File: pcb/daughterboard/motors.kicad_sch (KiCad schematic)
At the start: 20 parts, among them J10 Conn_01x04_Socket, J11 Conn_01x04_Socket, J12 Conn_01x04_Socket, J13 Conn_01x04_Socket, J14 Conn_01x04_Socket, J15 Conn_01x04_Socket, J16 Conn_01x04_Socket, J17 Conn_01x04_Socket, J18 Conn_01x04_Socket, J19 Conn_01x04_Socket, J2 Conn_01x04_Socket, J20 Conn_01x04_Socket, J21 Conn_01x04_Socket, J3 Conn_01x04_Socket, J4 Conn_01x04_Socket, J5 Conn_01x04_Socket, J6 Conn_01x04_Socket, J7 Conn_01x04_Socket, J8 Conn_01x04_Socket, J9 Conn_01x04_Socket

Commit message: added initial power lines
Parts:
- removed J2: Conn_01x04_Socket, A_HANU_FOOTPRINTS:52207-0633, symbol Connector:Conn_01x04_Socket
- added J22: Conn_01x04_Socket, A_HANU_FOOTPRINTS:52207-0633, symbol Connector:Conn_01x04_Socket
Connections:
- net PAD1_M1: now also J3.1 (Pin_1)
- net PAD1_M10: now also J12.1 (Pin_1); no longer J11.1 (Pin_1)
- net PAD1_M11: now also J13.1 (Pin_1); no longer J12.1 (Pin_1)
- net PAD1_M12: now also J14.1 (Pin_1); no longer J13.1 (Pin_1)
- net PAD1_M13: now also J15.1 (Pin_1); no longer J14.1 (Pin_1)
- net PAD1_M14: now also J16.1 (Pin_1); no longer J15.1 (Pin_1)
- net PAD1_M15: now also J17.1 (Pin_1); no longer J16.1 (Pin_1)
- net PAD1_M16: now also J18.1 (Pin_1); no longer J17.1 (Pin_1)
- net PAD1_M17: now also J19.1 (Pin_1); no longer J18.1 (Pin_1)
- net PAD1_M18: now also J20.1 (Pin_1); no longer J19.1 (Pin_1)
- net PAD1_M19: now also J21.1 (Pin_1); no longer J20.1 (Pin_1)
- net PAD1_M2: now also J4.1 (Pin_1); no longer J3.1 (Pin_1)
- net PAD1_M20: now also J22.1 (Pin_1); no longer J21.1 (Pin_1)
- net PAD1_M3: now also J5.1 (Pin_1); no longer J4.1 (Pin_1)
- net PAD1_M4: now also J6.1 (Pin_1); no longer J5.1 (Pin_1)
- net PAD1_M5: now also J7.1 (Pin_1); no longer J6.1 (Pin_1)
- net PAD1_M6: now also J8.1 (Pin_1); no longer J7.1 (Pin_1)
- net PAD1_M7: now also J9.1 (Pin_1); no longer J8.1 (Pin_1)
- net PAD1_M8: now also J10.1 (Pin_1); no longer J9.1 (Pin_1)
- net PAD1_M9: now also J11.1 (Pin_1); no longer J10.1 (Pin_1)
- net PAD2_M1: now also J3.2 (Pin_2)
- net PAD2_M10: now also J12.2 (Pin_2); no longer J11.2 (Pin_2)
- net PAD2_M11: now also J13.2 (Pin_2); no longer J12.2 (Pin_2)
- net PAD2_M12: now also J14.2 (Pin_2); no longer J13.2 (Pin_2)
- net PAD2_M13: now also J15.2 (Pin_2); no longer J14.2 (Pin_2)
- net PAD2_M14: now also J16.2 (Pin_2); no longer J15.2 (Pin_2)
- net PAD2_M15: now also J17.2 (Pin_2); no longer J16.2 (Pin_2)
- net PAD2_M16: now also J18.2 (Pin_2); no longer J17.2 (Pin_2)
- net PAD2_M17: now also J19.2 (Pin_2); no longer J18.2 (Pin_2)
- net PAD2_M18: now also J20.2 (Pin_2); no longer J19.2 (Pin_2)
- net PAD2_M19: now also J21.2 (Pin_2); no longer J20.2 (Pin_2)
- net PAD2_M2: now also J4.2 (Pin_2); no longer J3.2 (Pin_2)
- net PAD2_M20: now also J22.2 (Pin_2); no longer J21.2 (Pin_2)
- net PAD2_M3: now also J5.2 (Pin_2); no longer J4.2 (Pin_2)
- net PAD2_M4: now also J6.2 (Pin_2); no longer J5.2 (Pin_2)
- net PAD2_M5: now also J7.2 (Pin_2); no longer J6.2 (Pin_2)
- net PAD2_M6: now also J8.2 (Pin_2); no longer J7.2 (Pin_2)
- net PAD2_M7: now also J9.2 (Pin_2); no longer J8.2 (Pin_2)
- net PAD2_M8: now also J10.2 (Pin_2); no longer J9.2 (Pin_2)
- net PAD2_M9: now also J11.2 (Pin_2); no longer J10.2 (Pin_2)
- net PAD3_M1: now also J3.3 (Pin_3)
- net PAD3_M10: now also J12.3 (Pin_3); no longer J11.3 (Pin_3)
- net PAD3_M11: now also J13.3 (Pin_3); no longer J12.3 (Pin_3)
- net PAD3_M12: now also J14.3 (Pin_3); no longer J13.3 (Pin_3)
- net PAD3_M13: now also J15.3 (Pin_3); no longer J14.3 (Pin_3)
- net PAD3_M14: now also J16.3 (Pin_3); no longer J15.3 (Pin_3)
- net PAD3_M15: now also J17.3 (Pin_3); no longer J16.3 (Pin_3)
- net PAD3_M16: now also J18.3 (Pin_3); no longer J17.3 (Pin_3)
- net PAD3_M17: now also J19.3 (Pin_3); no longer J18.3 (Pin_3)
- net PAD3_M18: now also J20.3 (Pin_3); no longer J19.3 (Pin_3)
- net PAD3_M19: now also J21.3 (Pin_3); no longer J20.3 (Pin_3)
- net PAD3_M2: now also J4.3 (Pin_3); no longer J3.3 (Pin_3)
- net PAD3_M20: now also J22.3 (Pin_3); no longer J21.3 (Pin_3)
- net PAD3_M3: now also J5.3 (Pin_3); no longer J4.3 (Pin_3)
- net PAD3_M4: now also J6.3 (Pin_3); no longer J5.3 (Pin_3)
- net PAD3_M5: now also J7.3 (Pin_3); no longer J6.3 (Pin_3)
- net PAD3_M6: now also J8.3 (Pin_3); no longer J7.3 (Pin_3)
- net PAD3_M7: now also J9.3 (Pin_3); no longer J8.3 (Pin_3)
- net PAD3_M8: now also J10.3 (Pin_3); no longer J9.3 (Pin_3)
- net PAD3_M9: now also J11.3 (Pin_3); no longer J10.3 (Pin_3)
- net PAD4_M1: now also J3.4 (Pin_4)
- net PAD4_M10: now also J12.4 (Pin_4); no longer J11.4 (Pin_4)
- net PAD4_M11: now also J13.4 (Pin_4); no longer J12.4 (Pin_4)
- net PAD4_M12: now also J14.4 (Pin_4); no longer J13.4 (Pin_4)
- net PAD4_M13: now also J15.4 (Pin_4); no longer J14.4 (Pin_4)
- net PAD4_M14: now also J16.4 (Pin_4); no longer J15.4 (Pin_4)
- net PAD4_M15: now also J17.4 (Pin_4); no longer J16.4 (Pin_4)
- net PAD4_M16: now also J18.4 (Pin_4); no longer J17.4 (Pin_4)
- net PAD4_M17: now also J19.4 (Pin_4); no longer J18.4 (Pin_4)
- net PAD4_M18: now also J20.4 (Pin_4); no longer J19.4 (Pin_4)
- net PAD4_M19: now also J21.4 (Pin_4); no longer J20.4 (Pin_4)
- net PAD4_M2: now also J4.4 (Pin_4); no longer J3.4 (Pin_4)
- net PAD4_M20: now also J22.4 (Pin_4); no longer J21.4 (Pin_4)
- net PAD4_M3: now also J5.4 (Pin_4); no longer J4.4 (Pin_4)
- net PAD4_M4: now also J6.4 (Pin_4); no longer J5.4 (Pin_4)
- net PAD4_M5: now also J7.4 (Pin_4); no longer J6.4 (Pin_4)
- net PAD4_M6: now also J8.4 (Pin_4); no longer J7.4 (Pin_4)
- net PAD4_M7: now also J9.4 (Pin_4); no longer J8.4 (Pin_4)
- net PAD4_M8: now also J10.4 (Pin_4); no longer J9.4 (Pin_4)
- net PAD4_M9: now also J11.4 (Pin_4); no longer J10.4 (Pin_4)

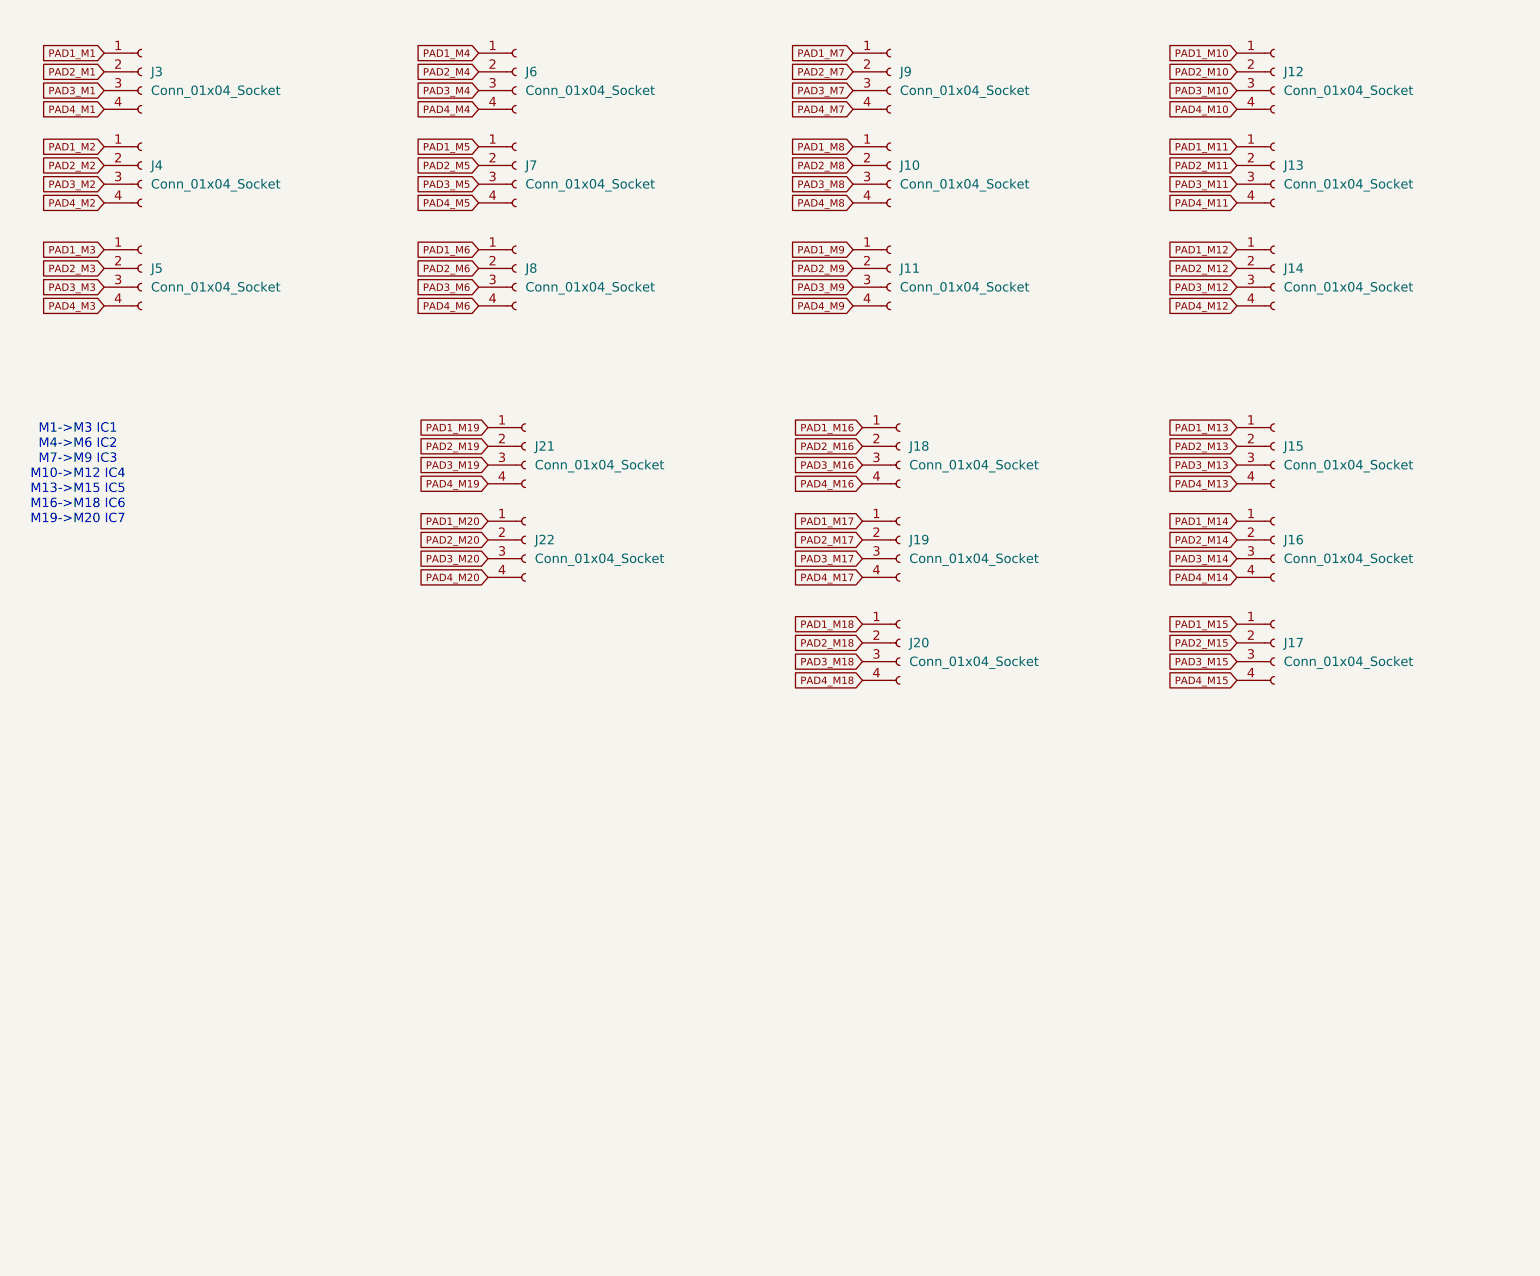
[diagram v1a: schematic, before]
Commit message: added routes for some motor-connectors
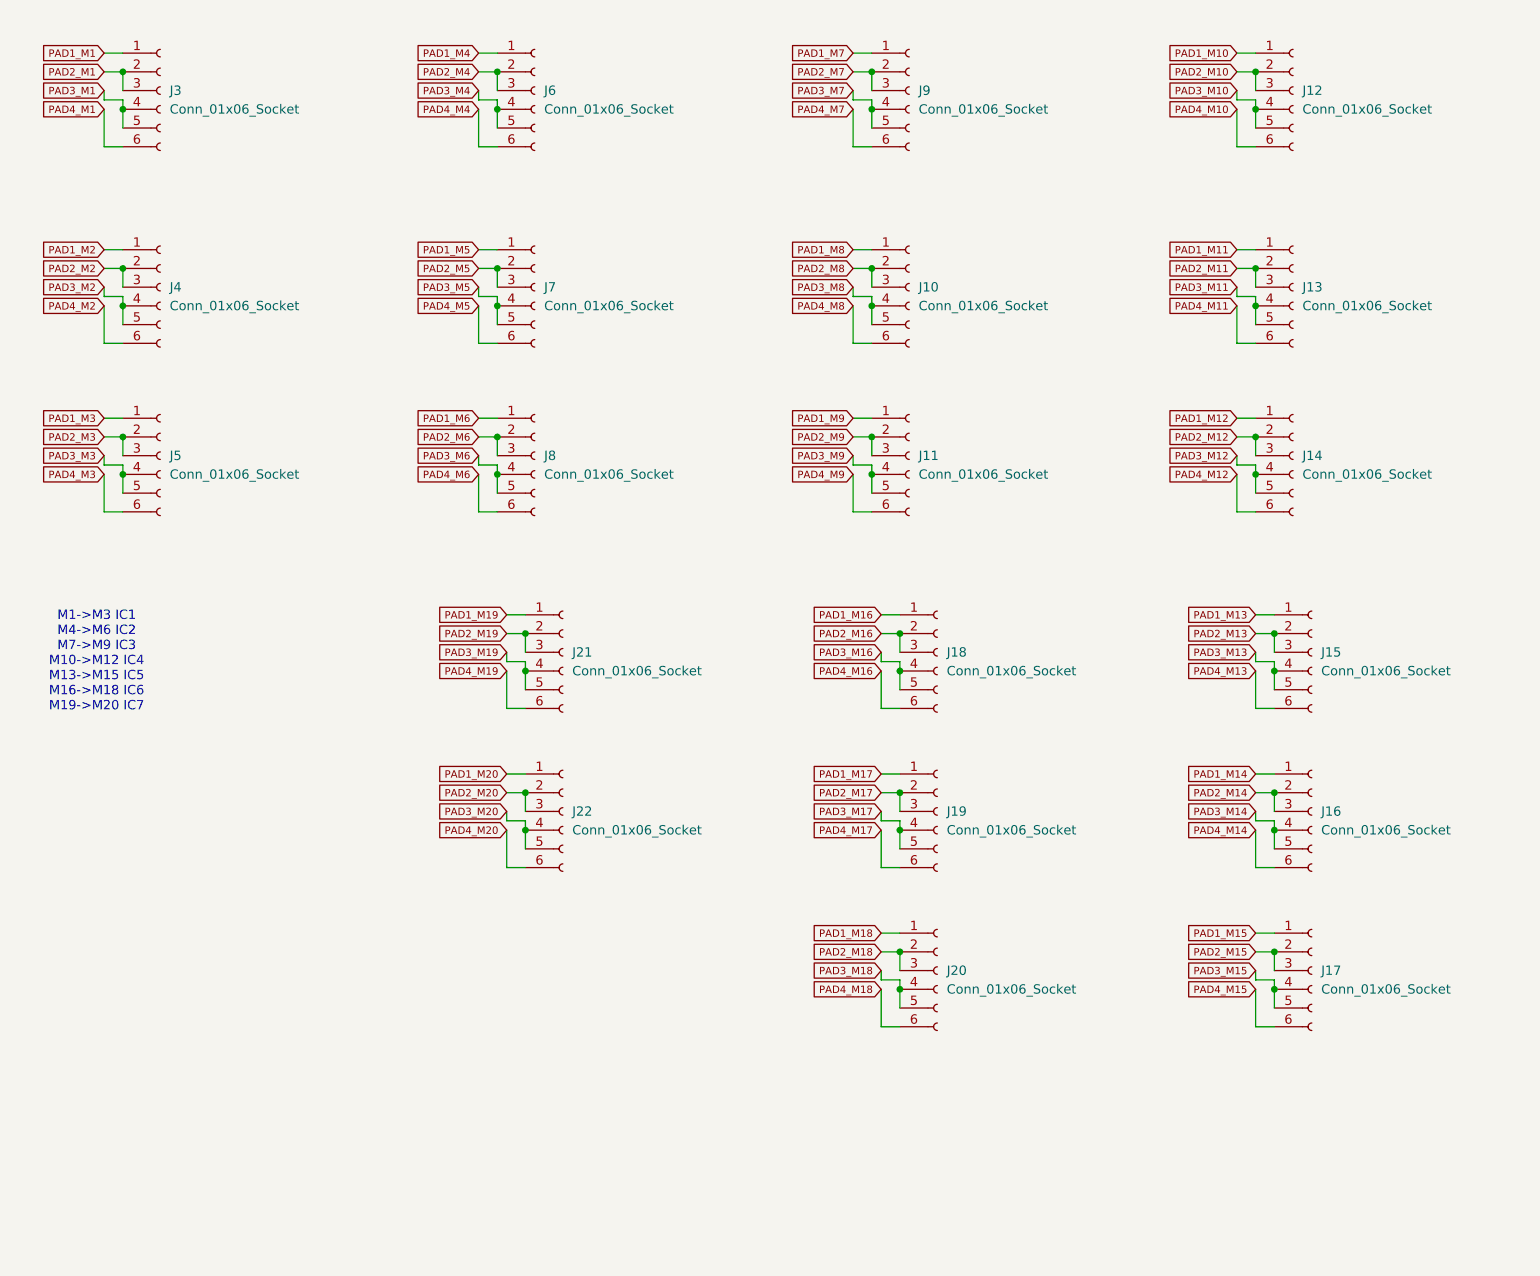
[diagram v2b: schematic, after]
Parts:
- removed J10, J11, J12, J13, J14, J15, J16, J17, J18, J19, J20, J21, J22, J3, J4, J5, J6, J7, J8, J9: Conn_01x04_Socket, A_HANU_FOOTPRINTS:52207-0633, symbol Connector:Conn_01x04_Socket
- added J10, J11, J12, J13, J14, J15, J16, J17, J18, J19, J20, J21, J22, J3, J4, J5, J6, J7, J8, J9: Conn_01x06_Socket, A_HANU_FOOTPRINTS:52207-0633, symbol Connector:Conn_01x06_Socket
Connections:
- net PAD1_M1: now also J3.1 (Pin_1)
- net PAD1_M10: now also J12.1 (Pin_1)
- net PAD1_M11: now also J13.1 (Pin_1)
- net PAD1_M12: now also J14.1 (Pin_1)
- net PAD1_M13: now also J15.1 (Pin_1)
- net PAD1_M14: now also J16.1 (Pin_1)
- net PAD1_M15: now also J17.1 (Pin_1)
- net PAD1_M16: now also J18.1 (Pin_1)
- net PAD1_M17: now also J19.1 (Pin_1)
- net PAD1_M18: now also J20.1 (Pin_1)
- net PAD1_M19: now also J21.1 (Pin_1)
- net PAD1_M2: now also J4.1 (Pin_1)
- net PAD1_M20: now also J22.1 (Pin_1)
- net PAD1_M3: now also J5.1 (Pin_1)
- net PAD1_M4: now also J6.1 (Pin_1)
- net PAD1_M5: now also J7.1 (Pin_1)
- net PAD1_M6: now also J8.1 (Pin_1)
- net PAD1_M7: now also J9.1 (Pin_1)
- net PAD1_M8: now also J10.1 (Pin_1)
- net PAD1_M9: now also J11.1 (Pin_1)
- net PAD2_M1: now also J3.2 (Pin_2), J3.3 (Pin_3)
- net PAD2_M10: now also J12.2 (Pin_2), J12.3 (Pin_3)
- net PAD2_M11: now also J13.2 (Pin_2), J13.3 (Pin_3)
- net PAD2_M12: now also J14.2 (Pin_2), J14.3 (Pin_3)
- net PAD2_M13: now also J15.2 (Pin_2), J15.3 (Pin_3)
- net PAD2_M14: now also J16.2 (Pin_2), J16.3 (Pin_3)
- net PAD2_M15: now also J17.2 (Pin_2), J17.3 (Pin_3)
- net PAD2_M16: now also J18.2 (Pin_2), J18.3 (Pin_3)
- net PAD2_M17: now also J19.2 (Pin_2), J19.3 (Pin_3)
- net PAD2_M18: now also J20.2 (Pin_2), J20.3 (Pin_3)
- net PAD2_M19: now also J21.2 (Pin_2), J21.3 (Pin_3)
- net PAD2_M2: now also J4.2 (Pin_2), J4.3 (Pin_3)
- net PAD2_M20: now also J22.2 (Pin_2), J22.3 (Pin_3)
- net PAD2_M3: now also J5.2 (Pin_2), J5.3 (Pin_3)
- net PAD2_M4: now also J6.2 (Pin_2), J6.3 (Pin_3)
- net PAD2_M5: now also J7.2 (Pin_2), J7.3 (Pin_3)
- net PAD2_M6: now also J8.2 (Pin_2), J8.3 (Pin_3)
- net PAD2_M7: now also J9.2 (Pin_2), J9.3 (Pin_3)
- net PAD2_M8: now also J10.2 (Pin_2), J10.3 (Pin_3)
- net PAD2_M9: now also J11.2 (Pin_2), J11.3 (Pin_3)
- net PAD3_M1: now also J3.4 (Pin_4), J3.5 (Pin_5)
- net PAD3_M10: now also J12.4 (Pin_4), J12.5 (Pin_5)
- net PAD3_M11: now also J13.4 (Pin_4), J13.5 (Pin_5)
- net PAD3_M12: now also J14.4 (Pin_4), J14.5 (Pin_5)
- net PAD3_M13: now also J15.4 (Pin_4), J15.5 (Pin_5)
- net PAD3_M14: now also J16.4 (Pin_4), J16.5 (Pin_5)
- net PAD3_M15: now also J17.4 (Pin_4), J17.5 (Pin_5)
- net PAD3_M16: now also J18.4 (Pin_4), J18.5 (Pin_5)
- net PAD3_M17: now also J19.4 (Pin_4), J19.5 (Pin_5)
- net PAD3_M18: now also J20.4 (Pin_4), J20.5 (Pin_5)
- net PAD3_M19: now also J21.4 (Pin_4), J21.5 (Pin_5)
- net PAD3_M2: now also J4.4 (Pin_4), J4.5 (Pin_5)
- net PAD3_M20: now also J22.4 (Pin_4), J22.5 (Pin_5)
- net PAD3_M3: now also J5.4 (Pin_4), J5.5 (Pin_5)
- net PAD3_M4: now also J6.4 (Pin_4), J6.5 (Pin_5)
- net PAD3_M5: now also J7.4 (Pin_4), J7.5 (Pin_5)
- net PAD3_M6: now also J8.4 (Pin_4), J8.5 (Pin_5)
- net PAD3_M7: now also J9.4 (Pin_4), J9.5 (Pin_5)
- net PAD3_M8: now also J10.4 (Pin_4), J10.5 (Pin_5)
- net PAD3_M9: now also J11.4 (Pin_4), J11.5 (Pin_5)
- net PAD4_M1: now also J3.6 (Pin_6)
- net PAD4_M10: now also J12.6 (Pin_6)
- net PAD4_M11: now also J13.6 (Pin_6)
- net PAD4_M12: now also J14.6 (Pin_6)
- net PAD4_M13: now also J15.6 (Pin_6)
- net PAD4_M14: now also J16.6 (Pin_6)
- net PAD4_M15: now also J17.6 (Pin_6)
- net PAD4_M16: now also J18.6 (Pin_6)
- net PAD4_M17: now also J19.6 (Pin_6)
- net PAD4_M18: now also J20.6 (Pin_6)
- net PAD4_M19: now also J21.6 (Pin_6)
- net PAD4_M2: now also J4.6 (Pin_6)
- net PAD4_M20: now also J22.6 (Pin_6)
- net PAD4_M3: now also J5.6 (Pin_6)
- net PAD4_M4: now also J6.6 (Pin_6)
- net PAD4_M5: now also J7.6 (Pin_6)
- net PAD4_M6: now also J8.6 (Pin_6)
- net PAD4_M7: now also J9.6 (Pin_6)
- net PAD4_M8: now also J10.6 (Pin_6)
- net PAD4_M9: now also J11.6 (Pin_6)

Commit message: Initial pcb design for daughterboard Added 3D models for components Modified the daughterboard to motherboard connectors Removed 220uF capacitors from the 5V5 power line
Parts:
- J10, J11, J12, J13, J14, J15, J16, J17, J18, J19, J20, J21, J22, J3, J4, J5, J6, J7, J8, J9: footprint A_HANU_FOOTPRINTS:52207-0633 -> 52207-0633:52207-0633
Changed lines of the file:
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@@
 			)
 		)
-		(property "Footprint" "A_HANU_FOOTPRINTS:52207-0633"
+		(property "Footprint" "52207-0633:52207-0633"
 			(at 199.39 107.95 0)
 			(hide yes)
@@
 			)
 		)
-		(property "Footprint" "A_HANU_FOOTPRINTS:52207-0633"
+		(property "Footprint" "52207-0633:52207-0633"
 			(at 93.98 31.75 0)
 			(hide yes)
@@
 			)
 		)
-		(property "Footprint" "A_HANU_FOOTPRINTS:52207-0633"
+		(property "Footprint" "52207-0633:52207-0633"
 			(at 43.18 58.42 0)
 			(hide yes)
@@
 			)
 		)
-		(property "Footprint" "A_HANU_FOOTPRINTS:52207-0633"
+		(property "Footprint" "52207-0633:52207-0633"
 			(at 148.59 107.95 0)
 			(hide yes)
@@
 			)
 		)
-		(property "Footprint" "A_HANU_FOOTPRINTS:52207-0633"
+		(property "Footprint" "52207-0633:52207-0633"
 			(at 144.78 58.42 0)
 			(hide yes)
@@
 			)
 		)
-		(property "Footprint" "A_HANU_FOOTPRINTS:52207-0633"
+		(property "Footprint" "52207-0633:52207-0633"
 			(at 148.59 151.13 0)
 			(hide yes)
@@
 			)
 		)
-		(property "Footprint" "A_HANU_FOOTPRINTS:52207-0633"
+		(property "Footprint" "52207-0633:52207-0633"
 			(at 196.85 31.75 0)
 			(hide yes)
@@
 			)
 		)
-		(property "Footprint" "A_HANU_FOOTPRINTS:52207-0633"
+		(property "Footprint" "52207-0633:52207-0633"
 			(at 196.85 58.42 0)
 			(hide yes)
@@
 			)
 		)
-		(property "Footprint" "A_HANU_FOOTPRINTS:52207-0633"
+		(property "Footprint" "52207-0633:52207-0633"
 			(at 43.18 81.28 0)
 			(hide yes)
@@
 			)
 		)
-		(property "Footprint" "A_HANU_FOOTPRINTS:52207-0633"
+		(property "Footprint" "52207-0633:52207-0633"
 			(at 148.59 129.54 0)
 			(hide yes)
@@
 			)
 		)
-		(property "Footprint" "A_HANU_FOOTPRINTS:52207-0633"
+		(property "Footprint" "52207-0633:52207-0633"
 			(at 196.85 81.28 0)
 			(hide yes)
@@
 			)
 		)
-		(property "Footprint" "A_HANU_FOOTPRINTS:52207-0633"
+		(property "Footprint" "52207-0633:52207-0633"
 			(at 199.39 151.13 0)
 			(hide yes)
@@
 			)
 		)
-		(property "Footprint" "A_HANU_FOOTPRINTS:52207-0633"
+		(property "Footprint" "52207-0633:52207-0633"
 			(at 93.98 81.28 0)
 			(hide yes)
@@
 			)
 		)
-		(property "Footprint" "A_HANU_FOOTPRINTS:52207-0633"
+		(property "Footprint" "52207-0633:52207-0633"
 			(at 199.39 129.54 0)
 			(hide yes)
@@
 			)
 		)
-		(property "Footprint" "A_HANU_FOOTPRINTS:52207-0633"
+		(property "Footprint" "52207-0633:52207-0633"
 			(at 93.98 58.42 0)
 			(hide yes)
@@
 			)
 		)
-		(property "Footprint" "A_HANU_FOOTPRINTS:52207-0633"
+		(property "Footprint" "52207-0633:52207-0633"
 			(at 144.78 31.75 0)
 			(hide yes)
@@
 			)
 		)
-		(property "Footprint" "A_HANU_FOOTPRINTS:52207-0633"
+		(property "Footprint" "52207-0633:52207-0633"
 			(at 43.18 31.75 0)
 			(hide yes)
@@
 			)
 		)
-		(property "Footprint" "A_HANU_FOOTPRINTS:52207-0633"
+		(property "Footprint" "52207-0633:52207-0633"
 			(at 144.78 81.28 0)
 			(hide yes)
@@
 			)
 		)
-		(property "Footprint" "A_HANU_FOOTPRINTS:52207-0633"
+		(property "Footprint" "52207-0633:52207-0633"
 			(at 97.79 107.95 0)
 			(hide yes)
@@
 			)
 		)
-		(property "Footprint" "A_HANU_FOOTPRINTS:52207-0633"
+		(property "Footprint" "52207-0633:52207-0633"
 			(at 97.79 129.54 0)
 			(hide yes)

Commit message: Final touches for the PCB order Added MPN, Description, checked footprints and 3D models Finished the BOM
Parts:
- J10, J11, J12, J13, J14, J15, J16, J17, J18, J19, J20, J21, J22, J3, J4, J5, J6, J7, J8, J9: Manufacturer_Name (none) -> Molex; Manufacturer_Part_Number (none) -> 52207-0633
